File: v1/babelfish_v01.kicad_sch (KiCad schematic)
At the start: 74 parts, among them J1 Conn_02x02_Odd_Even, J3 SWD, J5 IO_A, J7 USB_A, Q1 BSS138, SW1 K2-1836UQ-C3DW-06, U1 RP2040, U2 W25Q128JVS, U3 TPMCP1703T-5002E_CB, U4 GT-USB-7010ASV, U5 TPS2113ADRBR, U6 TPMCP1703T-3302E_CB, X1 X322512MSB4SI

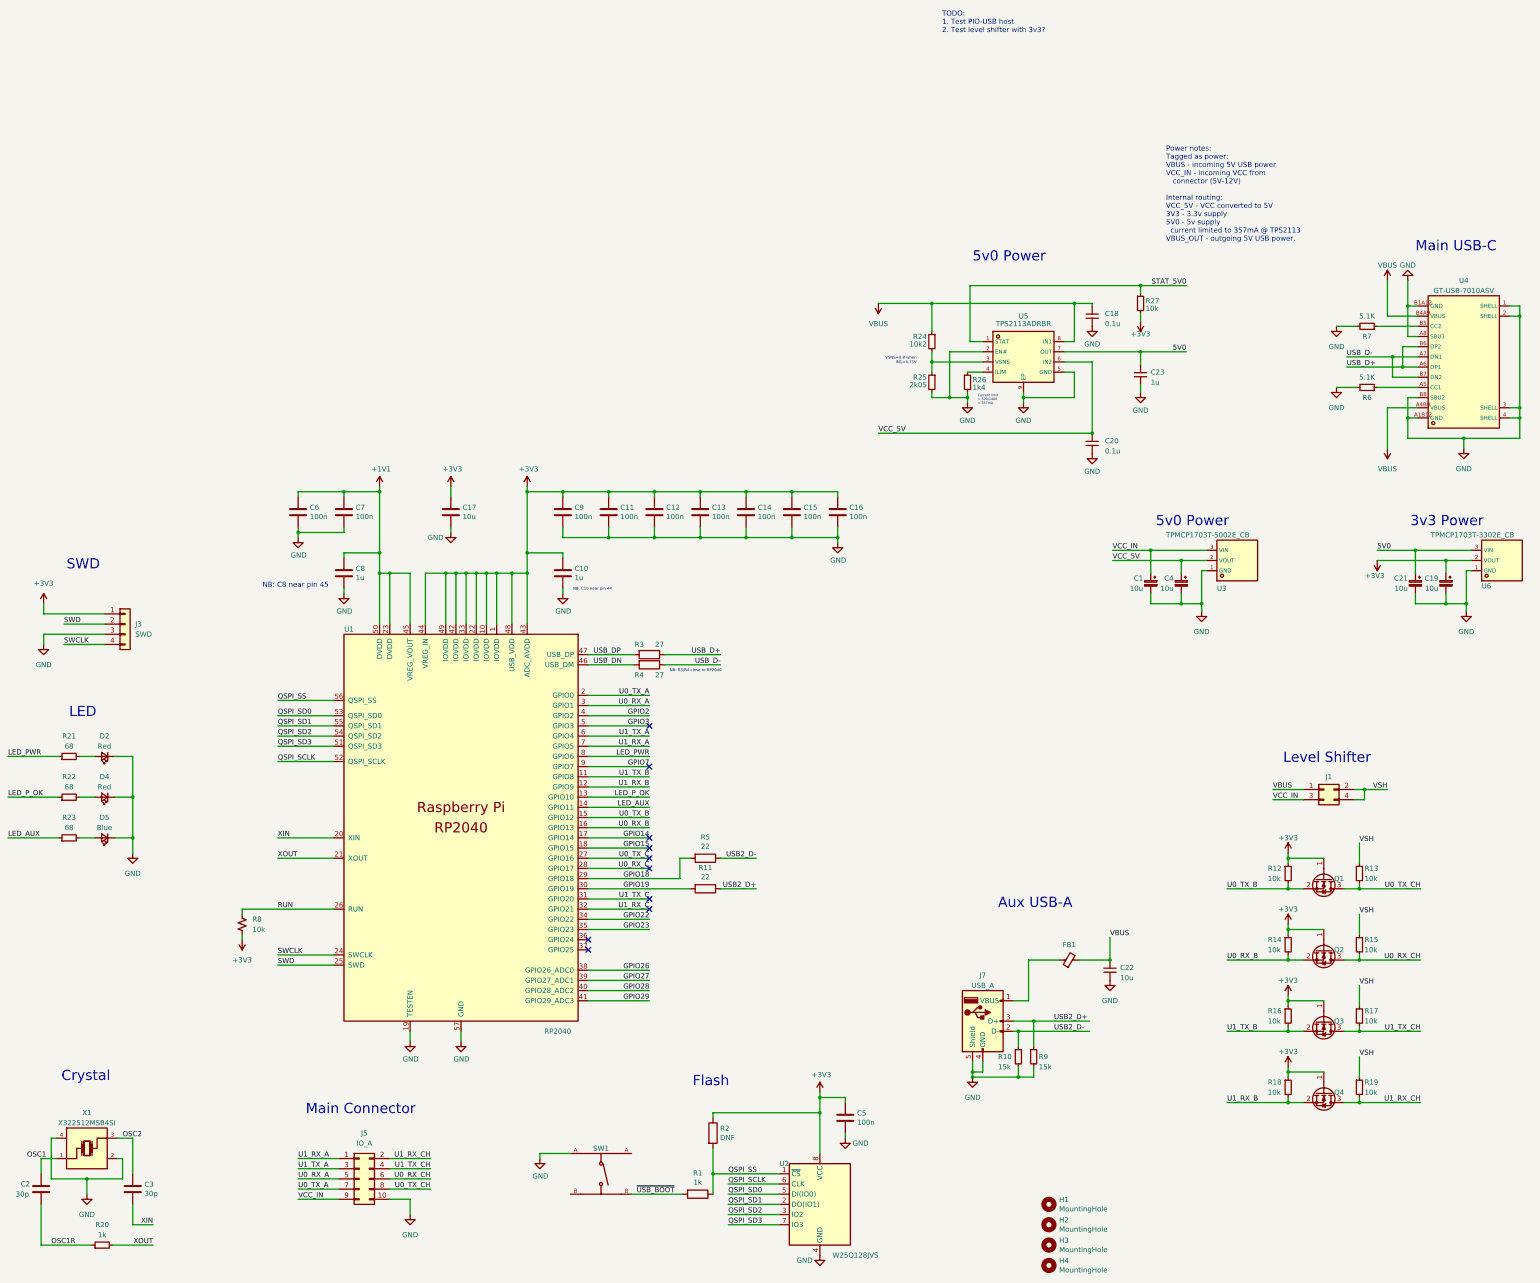
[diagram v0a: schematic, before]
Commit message: Moved files aroud. WIP new power section
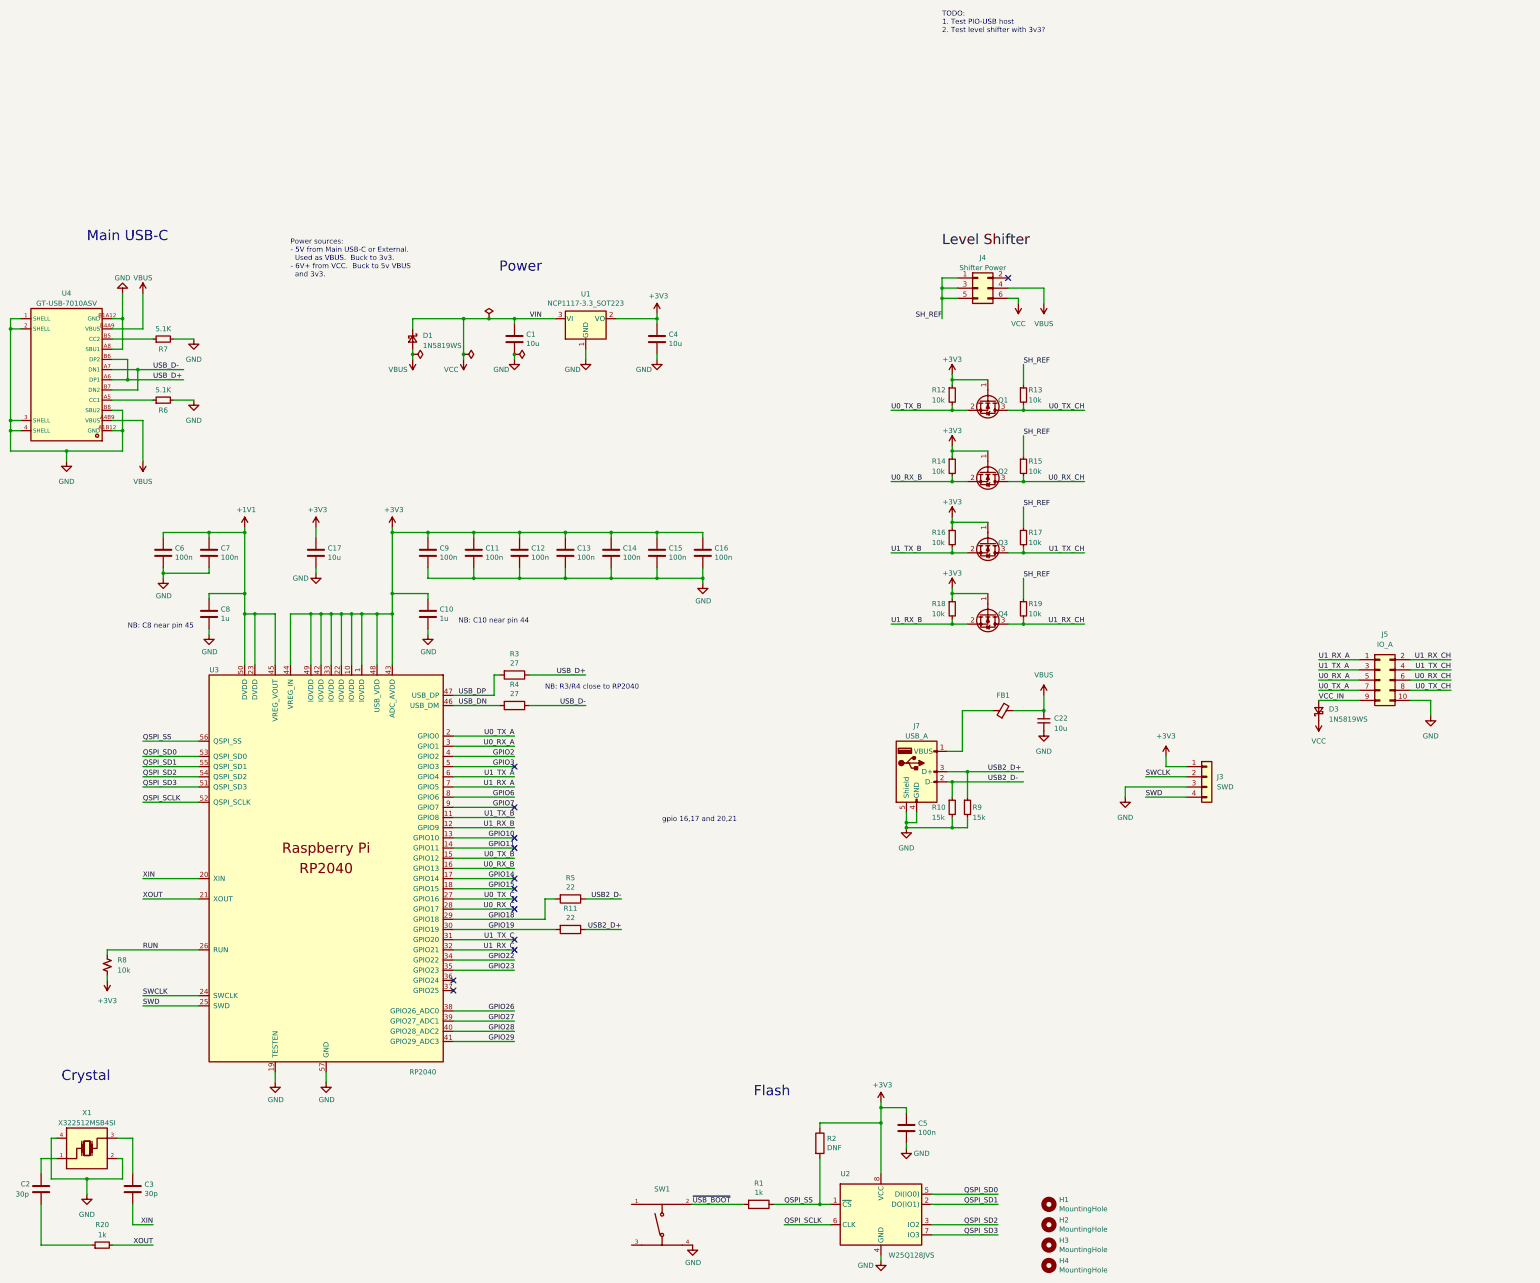
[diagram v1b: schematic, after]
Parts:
- removed C1, C19, C21, C4: 10u, symbol Device:C_Polarized_Small
- removed C18, C20: 0.1u, symbol Device:C_Small
- removed C23: 1u, symbol Device:C_Small
- removed D2, D4: Red, LED_SMD:LED_0603_1608Metric, symbol Device:LED_Small
- removed D5: Blue, LED_SMD:LED_0603_1608Metric, symbol Device:LED_Small
- removed J1: Conn_02x02_Odd_Even, Connector_PinHeader_2.54mm:PinHeader_2x02_P2.54mm_Vertical, symbol Connector_Generic:Conn_02x02_Odd_Even
- removed R21, R22, R23: 68, Resistor_SMD:R_0603_1608Metric, symbol Device:R_Small
- removed R24: 10k2, symbol Device:R_Small
- removed R25: 2k05, symbol Device:R_Small
- removed R26: 1k4, symbol Device:R_Small
- removed R27: 10k, symbol Device:R_Small
- removed U3: TPMCP1703T-5002E_CB, lcsc.pretty:SOT-23-3_L2.9-W1.6-P1.90-LS2.8-BR, symbol LCSC:TPMCP1703T-5002E_CB
- removed U5: TPS2113ADRBR, lcsc:SON-8_L3.0-W3.0-P0.65-LS3.0-BL-EP, symbol LCSC:TPS2113ADRBR
- removed U6: TPMCP1703T-3302E_CB, lcsc.pretty:SOT-23-3_L2.9-W1.6-P1.90-LS2.8-BR, symbol LCSC:TPMCP1703T-3302E_CB
- added C1, C4: 10u, Capacitor_SMD:C_0805_2012Metric, symbol Device:C
- added D1, D3: 1N5819WS, Diode_SMD:D_SOD-323, symbol Device:D_Schottky_Small
- added J4: Shifter Power, Connector_PinHeader_2.54mm:PinHeader_2x03_P2.54mm_Vertical, symbol Connector_Generic:Conn_02x03_Odd_Even
- added U1: NCP1117-3.3_SOT223, Package_TO_SOT_SMD:SOT-223-3_TabPin2, symbol Regulator_Linear:NCP1117-3.3_SOT223
- J3: footprint SnapEDA:490107670412 -> Connector_PinHeader_2.54mm:PinHeader_1x04_P2.54mm_Vertical
- SW1: value K2-1836UQ-C3DW-06 -> K2-1156SP-D5SW-05; footprint lcsc:SW-SMD_4P-L2.8-W2.4-P1.60-LS3.0 -> lcsc:SW-SMD_4P-L6.3-W6.2-P4.00-LS9.4-TL; symbol LCSC:K2-1836UQ-C3DW-06 -> LCSC:K2-1156SP-D5SW-05; LCSC C128935 -> C128948
- renumbered U1 to U3
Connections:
- net +3V3: now also C4.1, U1.2 (VO)
- net GND: now also SW1.4, C1.2, C4.2, U1.1 (GND); no longer SW1.A
- net SWCLK: now also J3.2 (Pin_2); no longer J3.4 (Pin_4)
- net SWD: now also J3.4 (Pin_4); no longer J3.2 (Pin_2)
- net VBUS: now also D1.2 (A), J4.4 (Pin_4)
- net VCC_IN: now also D3.2 (A)
- net ~{USB_BOOT}: now also SW1.2; no longer SW1.B
- net LED_AUX renamed GPIO11
- net LED_PWR renamed GPIO6
- net LED_P_OK renamed GPIO10
- net OSC1: no longer names the net of C2.1, X1.1 (OSC1)
- net OSC1R: no longer names the net of C2.2, R20.1
- net OSC2: no longer names the net of C3.1, X1.3 (OSC2)
- net VSH renamed SH_REF
- net SH_REF: now also J4.1 (Pin_1), J4.3 (Pin_3), J4.5 (Pin_5)
- new net VCC: C1.1, D1.1 (K), D3.1 (K), J4.6 (Pin_6), U1.3 (VI)
- no-connect marks 10 -> 13
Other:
- note added: "Power"
- note added: "Power sources: - 5V from Main USB-C or External. Used as VBUS. Buck to 3v3. - 6V+ from VCC. Buck to 5v VBUS and 3v3."
- note added: "gpio 16,17 and 20,21"
- note removed: "3v3 Power"
- note removed: "5v0 Power"
- note removed: "Aux USB-A"
- note removed: "Current limit = 500/1400 = 357mA"
- note removed: "LED"
- note removed: "Level Shifter"
- note removed: "Main Connector"
- note removed: "Power notes: Tagged as power: VBUS - incoming 5V USB power VCC_IN - incoming VCC from connector (5V-12V) Internal routing: VCC_5V - VCC converted to 5V 3V3 - 3.3v supply 5V0 - 5v supply current limited to 357mA @ TPS2113 VBUS_OUT - outgoing 5V USB power."
- note removed: "SWD"
- note removed: "VSNS=0.8 when IN1=4.75V"
- moved on the sheet: C10, C11, C12, C13, C14, C15, C16, C17, C22, C5, C6, C7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
